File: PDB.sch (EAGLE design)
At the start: 80 parts

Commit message: changed a bunch of PCB stuff
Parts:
- removed JP3: (no value), jumper:JP3QE
- added JP1: (no value), jumper:JP1Q
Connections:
- removed net BUCK_GND: JP3-1.1, JP3-1.2, VDD_IN.GND
- net GND: now also JP1.1, VDD_IN.GND; no longer JP3-2.1, JP3-2.2
- net µC_GND: now also JP1.2; no longer JP3-3.1, JP3-3.2
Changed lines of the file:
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@@
 <part name="SPI_OUT" library="master_library" deviceset="8-PIN-MOLEX-RA-FEMALE" device="" value="8-PIN-MOLEX-RA-FEMALE"/>
 <part name="U$4" library="master_library" deviceset="1410-L1" device=""/>
-<part name="JP3" library="jumper" library_urn="urn:adsk.eagle:library:252" deviceset="JP3QE" device="" package3d_urn="urn:adsk.eagle:package:15460/1"/>
 <part name="JP2" library="jumper" library_urn="urn:adsk.eagle:library:252" deviceset="JP2E" device="" package3d_urn="urn:adsk.eagle:package:15452/1"/>
 <part name="SUPPLY5" library="supply2" library_urn="urn:adsk.eagle:library:372" deviceset="GND" device=""/>
+<part name="JP1" library="jumper" library_urn="urn:adsk.eagle:library:252" deviceset="JP1Q" device="" package3d_urn="urn:adsk.eagle:package:15455/1"/>
 </parts>
 <sheets>
@@
 <instance part="SPI_OUT" gate="G$1" x="93.98" y="114.3"/>
 <instance part="U$4" gate="G$1" x="19.812" y="48.514" rot="R270"/>
-<instance part="JP3" gate="-1" x="238.76" y="101.6"/>
-<instance part="JP3" gate="-2" x="248.92" y="101.6"/>
-<instance part="JP3" gate="-3" x="259.08" y="101.6"/>
 <instance part="JP2" gate="1" x="215.9" y="203.2"/>
 <instance part="SUPPLY5" gate="GND" x="236.466840625" y="171.93440625">
 <attribute name="VALUE" x="234.561840625" y="168.75940625" size="1.778" layer="96"/>
 </instance>
+<instance part="JP1" gate="A" x="254" y="111.76" rot="R90"/>
 </instances>
 <busses>
@@
 </segment>
 <segment>
-<pinref part="JP3" gate="-2" pin="1"/>
-<wire x1="248.92" y1="99.06" x2="248.92" y2="96.52" width="0.1524" layer="91"/>
-<label x="248.92" y="91.44" size="1.778" layer="95" rot="R90"/>
-</segment>
-<segment>
-<pinref part="JP3" gate="-2" pin="2"/>
-<wire x1="251.46" y1="99.06" x2="251.46" y2="96.52" width="0.1524" layer="91"/>
-<label x="251.46" y="91.44" size="1.778" layer="95" rot="R90"/>
-</segment>
-<segment>
 <pinref part="R23" gate="G$1" pin="2"/>
 <pinref part="SUPPLY5" gate="GND" pin="GND"/>
 <wire x1="236.466840625" y1="174.47440625" x2="231.409840625" y2="174.47440625" width="0.1524" layer="91"/>
 <wire x1="231.409840625" y1="174.47440625" x2="231.409840625" y2="174.82840625" width="0.1524" layer="91"/>
+</segment>
+<segment>
+<pinref part="VDD_IN" gate="G$1" pin="GND"/>
+<wire x1="243.84" y1="127" x2="238.76" y2="127" width="0.1524" layer="91"/>
+<label x="238.76" y="127" size="1.778" layer="95" rot="R180" xref="yes"/>
+</segment>
+<segment>
+<pinref part="JP1" gate="A" pin="1"/>
+<wire x1="261.62" y1="111.76" x2="264.16" y2="111.76" width="0.1524" layer="91"/>
+<label x="264.16" y="111.76" size="1.778" layer="95"/>
 </segment>
 </net>
@@
 </segment>
 <segment>
-<pinref part="JP3" gate="-3" pin="1"/>
-<wire x1="259.08" y1="99.06" x2="259.08" y2="96.52" width="0.1524" layer="91"/>
-<label x="259.08" y="86.36" size="1.778" layer="95" rot="R90"/>
-</segment>
-<segment>
-<pinref part="JP3" gate="-3" pin="2"/>
-<wire x1="261.62" y1="99.06" x2="261.62" y2="96.52" width="0.1524" layer="91"/>
-<label x="261.62" y="86.36" size="1.778" layer="95" rot="R90"/>
+<pinref part="JP1" gate="A" pin="2"/>
+<wire x1="246.38" y1="111.76" x2="243.84" y2="111.76" width="0.1524" layer="91"/>
+<label x="233.68" y="111.76" size="1.778" layer="95"/>
 </segment>
 </net>
@@
 </segment>
 </net>
-<net name="BUCK_GND" class="0">
-<segment>
-<pinref part="VDD_IN" gate="G$1" pin="GND"/>
-<wire x1="243.84" y1="127" x2="238.76" y2="127" width="0.1524" layer="91"/>
-<label x="238.76" y="127" size="1.778" layer="95" rot="R180" xref="yes"/>
-</segment>
-<segment>
-<pinref part="JP3" gate="-1" pin="1"/>
-<wire x1="238.76" y1="99.06" x2="238.76" y2="96.52" width="0.1524" layer="91"/>
-<label x="238.76" y="83.82" size="1.778" layer="95" rot="R90"/>
-</segment>
-<segment>
-<pinref part="JP3" gate="-1" pin="2"/>
-<wire x1="241.3" y1="99.06" x2="241.3" y2="96.52" width="0.1524" layer="91"/>
-<label x="241.3" y="83.82" size="1.778" layer="95" rot="R90"/>
-</segment>
-</net>

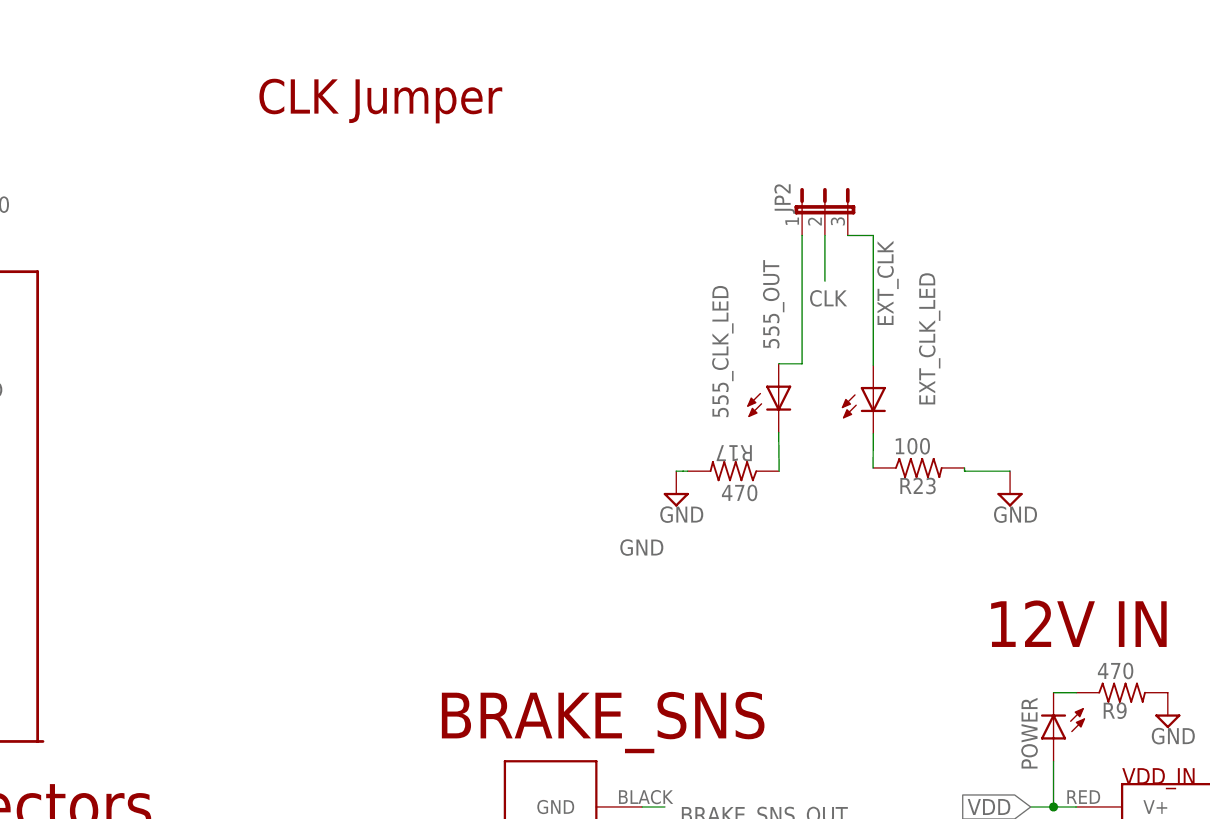
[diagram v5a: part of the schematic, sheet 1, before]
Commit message: close to final pcb layout, not yet routed
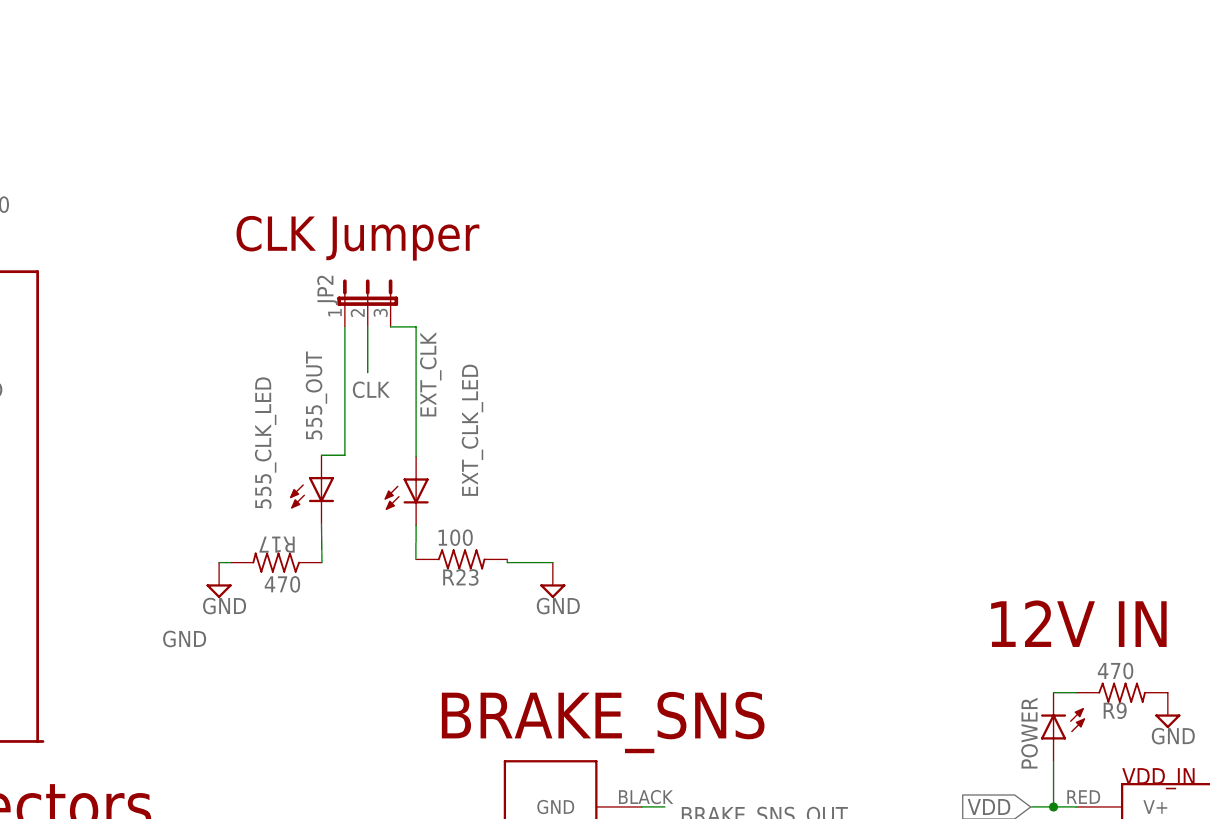
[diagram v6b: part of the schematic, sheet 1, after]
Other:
- moved on the sheet: 555_CLK_LED, EXT_CLK_LED, JP2, R17, R23
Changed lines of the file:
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@@
 <text x="83.02" y="219.12" size="3.81" layer="94">TRACO SPI Power</text>
 <text x="-115.5" y="138.06" size="3.81" layer="94">555 Voltage Reg</text>
-<text x="152.8" y="214.2" size="3.81" layer="94">CLK Jumper</text>
+<text x="150.26" y="198.96" size="3.81" layer="94">CLK Jumper</text>
 <text x="17.2" y="140" size="3.81" layer="94">SPI BUS</text>
 </plain>
@@
 <attribute name="VALUE" x="252.095" y="144.145" size="1.778" layer="96"/>
 </instance>
-<instance part="555_CLK_LED" gate="G$1" x="210.76091875" y="183.861025" smashed="yes">
-<attribute name="NAME" x="205.17291875" y="180.305025" size="1.778" layer="95" rot="R90"/>
-<attribute name="VALUE" x="216.47591875" y="179.289025" size="1.778" layer="96" rot="R90"/>
-</instance>
-<instance part="R17" gate="G$1" x="205.732840625" y="174.47440625" smashed="yes" rot="R180">
-<attribute name="NAME" x="207.996515625" y="177.36456875" size="1.778" layer="95" rot="SR180"/>
-<attribute name="VALUE" x="208.53504375" y="172.94846875" size="1.778" layer="96" rot="R180"/>
-</instance>
-<instance part="SUPPLY17" gate="GND" x="199.382840625" y="171.93440625">
-<attribute name="VALUE" x="197.477840625" y="168.75940625" size="1.778" layer="96"/>
-</instance>
-<instance part="EXT_CLK_LED" gate="G$1" x="221.27491875" y="183.707025" smashed="yes">
-<attribute name="NAME" x="228.15591875" y="181.675025" size="1.778" layer="95" rot="R90"/>
-<attribute name="VALUE" x="226.98991875" y="179.135025" size="1.778" layer="96" rot="R90"/>
-</instance>
-<instance part="R23" gate="G$1" x="226.329840625" y="174.82840625" smashed="yes">
-<attribute name="NAME" x="224.066165625" y="171.93824375" size="1.778" layer="95" rot="SR0"/>
-<attribute name="VALUE" x="223.5276375" y="176.35434375" size="1.778" layer="96"/>
+<instance part="555_CLK_LED" gate="G$1" x="159.96091875" y="173.701025" smashed="yes">
+<attribute name="NAME" x="154.37291875" y="170.145025" size="1.778" layer="95" rot="R90"/>
+<attribute name="VALUE" x="165.67591875" y="169.129025" size="1.778" layer="96" rot="R90"/>
+</instance>
+<instance part="R17" gate="G$1" x="154.932840625" y="164.31440625" smashed="yes" rot="R180">
+<attribute name="NAME" x="157.196515625" y="167.20456875" size="1.778" layer="95" rot="SR180"/>
+<attribute name="VALUE" x="157.73504375" y="162.78846875" size="1.778" layer="96" rot="R180"/>
+</instance>
+<instance part="SUPPLY17" gate="GND" x="148.582840625" y="161.77440625">
+<attribute name="VALUE" x="146.677840625" y="158.59940625" size="1.778" layer="96"/>
+</instance>
+<instance part="EXT_CLK_LED" gate="G$1" x="170.47491875" y="173.547025" smashed="yes">
+<attribute name="NAME" x="177.35591875" y="171.515025" size="1.778" layer="95" rot="R90"/>
+<attribute name="VALUE" x="176.18991875" y="168.975025" size="1.778" layer="96" rot="R90"/>
+</instance>
+<instance part="R23" gate="G$1" x="175.529840625" y="164.66840625" smashed="yes">
+<attribute name="NAME" x="173.266165625" y="161.77824375" size="1.778" layer="95" rot="SR0"/>
+<attribute name="VALUE" x="172.7276375" y="166.19434375" size="1.778" layer="96"/>
 </instance>
 <instance part="R24" gate="G$1" x="107.235" y="182.65"/>
@@
 <instance part="SPI_OUT" gate="G$1" x="93.98" y="114.3"/>
 <instance part="U$4" gate="G$1" x="19.812" y="48.514" rot="R270"/>
-<instance part="JP2" gate="1" x="215.9" y="203.2"/>
-<instance part="SUPPLY5" gate="GND" x="236.466840625" y="171.93440625">
-<attribute name="VALUE" x="234.561840625" y="168.75940625" size="1.778" layer="96"/>
+<instance part="JP2" gate="1" x="165.1" y="193.04"/>
+<instance part="SUPPLY5" gate="GND" x="185.666840625" y="161.77440625">
+<attribute name="VALUE" x="183.761840625" y="158.59940625" size="1.778" layer="96"/>
 </instance>
 <instance part="JP1" gate="A" x="254" y="111.76" rot="R90"/>
@@
 <pinref part="SUPPLY17" gate="GND" pin="GND"/>
 <pinref part="R17" gate="G$1" pin="2"/>
-<wire x1="200.652840625" y1="174.47440625" x2="200.144840625" y2="174.47440625" width="0.1524" layer="91"/>
-<wire x1="200.144840625" y1="174.47440625" x2="199.382840625" y2="174.47440625" width="0.1524" layer="91"/>
-<label x="193.04" y="165.1" size="1.778" layer="95"/>
+<wire x1="149.852840625" y1="164.31440625" x2="149.344840625" y2="164.31440625" width="0.1524" layer="91"/>
+<wire x1="149.344840625" y1="164.31440625" x2="148.582840625" y2="164.31440625" width="0.1524" layer="91"/>
+<label x="142.24" y="154.94" size="1.778" layer="95"/>
 </segment>
 <segment>
@@
 <pinref part="R23" gate="G$1" pin="2"/>
 <pinref part="SUPPLY5" gate="GND" pin="GND"/>
-<wire x1="236.466840625" y1="174.47440625" x2="231.409840625" y2="174.47440625" width="0.1524" layer="91"/>
-<wire x1="231.409840625" y1="174.47440625" x2="231.409840625" y2="174.82840625" width="0.1524" layer="91"/>
+<wire x1="185.666840625" y1="164.31440625" x2="180.609840625" y2="164.31440625" width="0.1524" layer="91"/>
+<wire x1="180.609840625" y1="164.31440625" x2="180.609840625" y2="164.66840625" width="0.1524" layer="91"/>
 </segment>
 <segment>
@@
 <pinref part="JP2" gate="1" pin="1"/>
 <pinref part="555_CLK_LED" gate="G$1" pin="A"/>
-<wire x1="213.36" y1="200.66" x2="213.36" y2="186.401025" width="0.1524" layer="91"/>
-<wire x1="213.36" y1="186.401025" x2="210.76091875" y2="186.401025" width="0.1524" layer="91"/>
-<label x="210.82" y="187.96" size="1.778" layer="95" rot="R90"/>
+<wire x1="162.56" y1="190.5" x2="162.56" y2="176.241025" width="0.1524" layer="91"/>
+<wire x1="162.56" y1="176.241025" x2="159.96091875" y2="176.241025" width="0.1524" layer="91"/>
+<label x="160.02" y="177.8" size="1.778" layer="95" rot="R90"/>
 </segment>
 </net>
@@
 <segment>
 <pinref part="JP2" gate="1" pin="3"/>
-<wire x1="218.44" y1="200.66" x2="221.27491875" y2="200.66" width="0.1524" layer="91"/>
+<wire x1="167.64" y1="190.5" x2="170.47491875" y2="190.5" width="0.1524" layer="91"/>
 <pinref part="EXT_CLK_LED" gate="G$1" pin="A"/>
-<wire x1="221.27491875" y1="200.66" x2="221.27491875" y2="186.247025" width="0.1524" layer="91"/>
-<label x="223.52" y="190.5" size="1.778" layer="95" rot="R90"/>
+<wire x1="170.47491875" y1="190.5" x2="170.47491875" y2="176.087025" width="0.1524" layer="91"/>
+<label x="172.72" y="180.34" size="1.778" layer="95" rot="R90"/>
 </segment>
 </net>
@@
 <segment>
 <pinref part="JP2" gate="1" pin="2"/>
-<wire x1="215.9" y1="200.66" x2="215.9" y2="195.58" width="0.1524" layer="91"/>
-<label x="214.122" y="192.786" size="1.778" layer="95"/>
+<wire x1="165.1" y1="190.5" x2="165.1" y2="185.42" width="0.1524" layer="91"/>
+<label x="163.322" y="182.626" size="1.778" layer="95"/>
 </segment>
 </net>
@@
 <pinref part="555_CLK_LED" gate="G$1" pin="C"/>
 <pinref part="R17" gate="G$1" pin="1"/>
-<wire x1="210.812840625" y1="174.47440625" x2="210.76091875" y2="178.781025" width="0.1524" layer="91"/>
+<wire x1="160.012840625" y1="164.31440625" x2="159.96091875" y2="168.621025" width="0.1524" layer="91"/>
 </segment>
 </net>
@@
 <pinref part="EXT_CLK_LED" gate="G$1" pin="C"/>
 <pinref part="R23" gate="G$1" pin="1"/>
-<wire x1="221.249840625" y1="174.82840625" x2="221.27491875" y2="178.627025" width="0.1524" layer="91"/>
-</segment>
-</net>
+<wire x1="170.449840625" y1="164.66840625" x2="170.47491875" y2="168.467025" width="0.1524" layer="91"/>
+</segment>
+</net>

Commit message: board planes layout
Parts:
- removed EXT_CLK_LED, LED_ADD1, LED_ADD2: (no value), led:LEDCHIPLED_0805
- removed U$4: 1410-L1, master_library:1410-L1
- added _ADD1, _ADD2, _EXT_CLK: (no value), led:LEDCHIPLED_0805
- ADD1, ADD2, BRAKE, HAZ_L, HAZ_R, HEAD, REAR, WIPER_: value PSMN039-100YS -> NCV8405ADPAK-3PIN; device nxp_60:PSMN039-100YS -> master_library:NCV8405ADPAK-3PIN
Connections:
- removed net 10V_SAFE: 555.R, 555.V+, C4.+, LM2940.OUT, R10.2
- removed net OUT: D2.C, U$4.OUT, WIPER_OUT.V+
- removed net TIMER_GND: HAZ_L.S, HAZ_R.S, R4.2, R5.2
- new net 10V_REG: 555.R, 555.V+, ADD1_.S, ADD2_.S, C4.+, HEADLIGHTS.P, LM2940.OUT, R10.2, REARLIGHTS.P, WIPER.P
- net 5V_REG: now also VDD_IN1.V+
- net EXT_CLK: now also _EXT_CLK.A; no longer EXT_CLK_LED.A
- net GND: now also HAZ_L.S, HAZ_R.S, R4.2, R5.2
- net N$3: now also _EXT_CLK.C; no longer EXT_CLK_LED.C
- net N$4: now also _ADD1.C; no longer LED_ADD1.C
- net N$5: now also _ADD2.C; no longer LED_ADD2.C
- net VDD: now also D2.C, WIPER_OUT.V+; no longer ADD1_.S, ADD2_.S, HEADLIGHTS.P, REARLIGHTS.P, U$4.IN, WIPER.P
- net µC_5V: no longer VDD_IN1.V+
- net µC_ADD_1: now also _ADD1.A; no longer LED_ADD1.A
- net µC_ADD_2: now also _ADD2.A; no longer LED_ADD2.A
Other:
- moved on the sheet: 555, 555_CLK_LED, ADD1_, ADD1_OUT, ADD2_, ADD2_OUT, BRAKE_OUT, C1, C10, C2, C3, C4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

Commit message: PCB layout
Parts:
- removed R22: 470, rcl:R-US_R3225
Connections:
- removed net Q: 555.Q, R22.1
- net 555_OUT: now also 555.Q; no longer R22.2
